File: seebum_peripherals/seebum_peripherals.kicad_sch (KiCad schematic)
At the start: 33 parts, among them J101 Conn_01x06_Socket, J102 Conn_01x06_Socket, J103 Conn_01x03_Socket, J104 Conn_01x02_Socket, J105 Conn_01x02_Socket, J106 Conn_01x07_Socket, J107 Conn_01x04_Socket, J108 Conn_01x03_Socket, J109 Conn_02x10_Odd_Even, J110 Conn_02x10_Odd_Even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

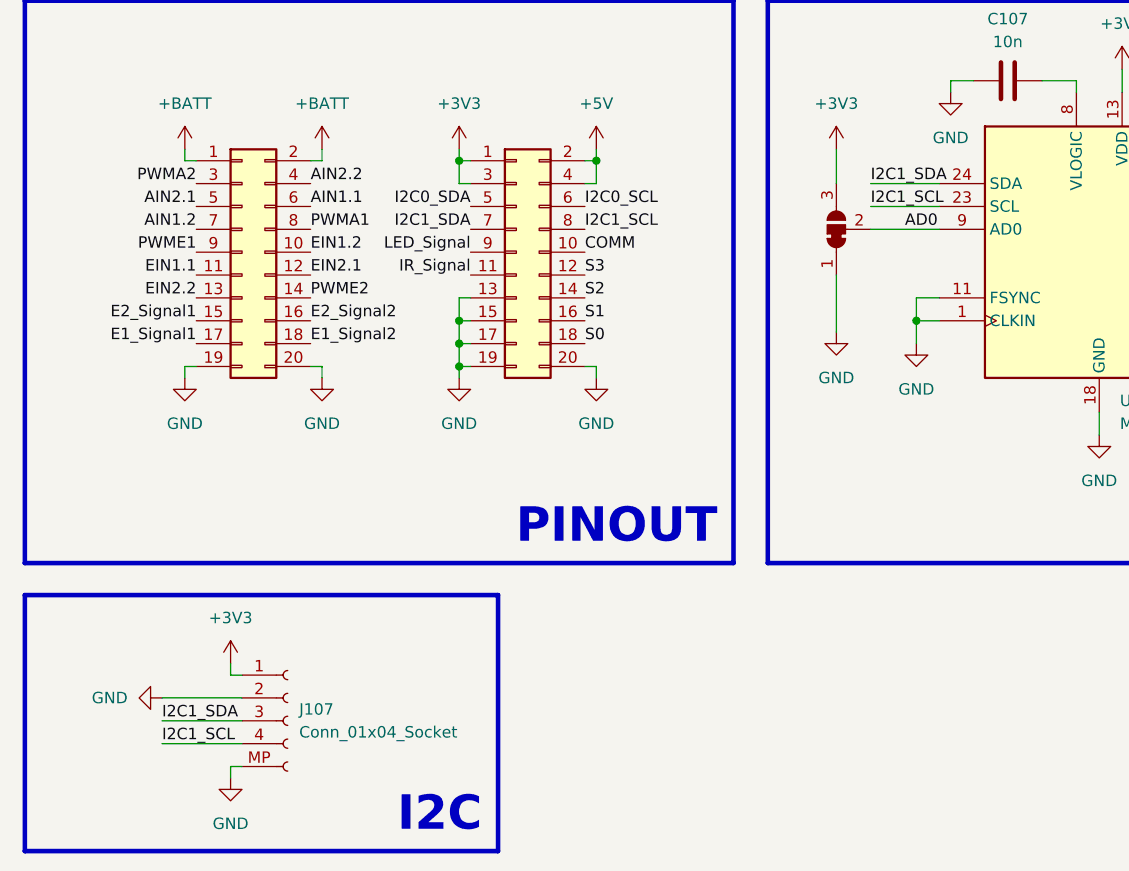
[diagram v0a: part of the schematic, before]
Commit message: Feat: fix I2C and silkscreen
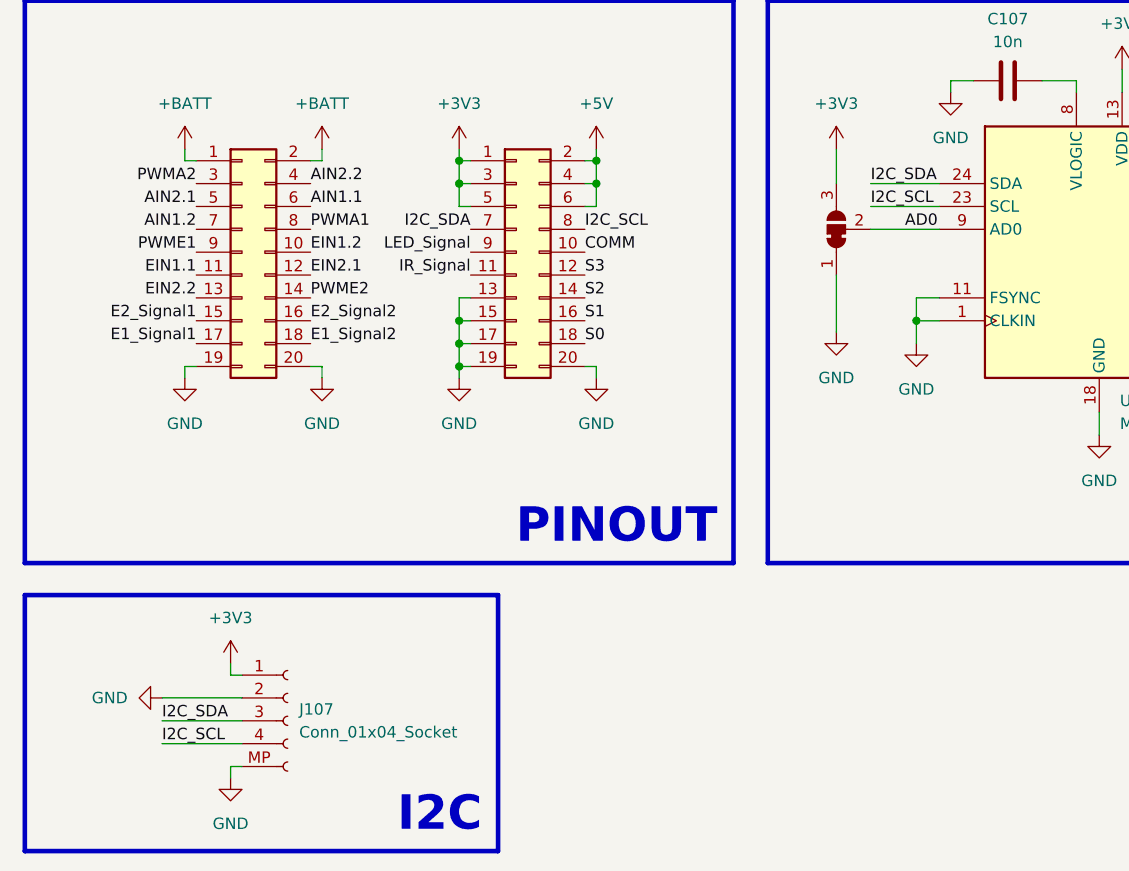
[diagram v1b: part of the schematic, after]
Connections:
- net I2C0_SCL is gone; now on net +5V: J110.6 (Pin_6)
- net I2C0_SDA is gone; now on net +3V3: J110.5 (Pin_5)
- net I2C1_SCL renamed I2C_SCL
- net I2C1_SDA renamed I2C_SDA
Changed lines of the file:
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@@
 	(paper "A4")
+	(junction
+		(at 184.15 120.65)
+		(diameter 0)
+		(color 0 0 0 0)
+	)
 	(junction
 		(at 241.3 83.82)
@@
 	)
 	(junction
+		(at 168.91 120.65)
+		(diameter 0)
+		(color 0 0 0 0)
+	)
+	(junction
 		(at 180.34 25.4)
 		(diameter 0)
@@
 	(wire
 		(pts
+			(xy 170.18 123.19) (xy 168.91 123.19)
+		)
+		(stroke
+			(width 0)
+			(type default)
+		)
+	)
+	(wire
+		(pts
 			(xy 271.78 133.35) (xy 271.78 137.16)
 		)
@@
 	(wire
 		(pts
+			(xy 184.15 123.19) (xy 184.15 120.65)
+		)
+		(stroke
+			(width 0)
+			(type default)
+		)
+	)
+	(wire
+		(pts
 			(xy 266.7 146.05) (xy 266.7 147.32)
 		)
@@
 	(wire
 		(pts
+			(xy 182.88 123.19) (xy 184.15 123.19)
+		)
+		(stroke
+			(width 0)
+			(type default)
+		)
+	)
+	(wire
+		(pts
 			(xy 260.35 135.89) (xy 260.35 137.16)
 		)
@@
 		(pts
 			(xy 264.16 111.76) (xy 264.16 113.03)
+		)
+		(stroke
+			(width 0)
+			(type default)
+		)
+	)
+	(wire
+		(pts
+			(xy 168.91 123.19) (xy 168.91 120.65)
 		)
 		(stroke
@@
 		)
 	)
-	(label "I2C1_SCL"
+	(label "I2C_SCL"
 		(at 214.63 123.19 0)
 		(fields_autoplaced yes)
@@
 		)
 	)
-	(label "I2C1_SCL"
+	(label "I2C_SCL"
 		(at 182.88 125.73 0)
 		(fields_autoplaced yes)
@@
 		)
 	)
-	(label "I2C1_SDA"
+	(label "I2C_SDA"
 		(at 135.89 180.34 0)
 		(fields_autoplaced yes)
@@
 		)
 	)
-	(label "I2C1_SDA"
+	(label "I2C_SDA"
 		(at 170.18 125.73 180)
 		(fields_autoplaced yes)
@@
 		)
 	)
-	(label "I2C0_SDA"
-		(at 170.18 123.19 180)
-		(fields_autoplaced yes)
-		(effects
-			(font
-				(size 1.27 1.27)
-			)
-			(justify right bottom)
-		)
-	)
-	(label "I2C1_SCL"
+	(label "I2C_SCL"
 		(at 135.89 182.88 0)
 		(fields_autoplaced yes)
@@
 		)
 	)
-	(label "I2C1_SDA"
+	(label "I2C_SDA"
 		(at 214.63 120.65 0)
 		(fields_autoplaced yes)
@@
 		)
 	)
-	(label "I2C0_SCL"
-		(at 182.88 123.19 0)
-		(fields_autoplaced yes)
-		(effects
-			(font
-				(size 1.27 1.27)
-			)
-			(justify left bottom)
-		)
-	)
